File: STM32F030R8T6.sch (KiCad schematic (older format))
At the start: 1 part, among them U1 STM32F030R8Tx

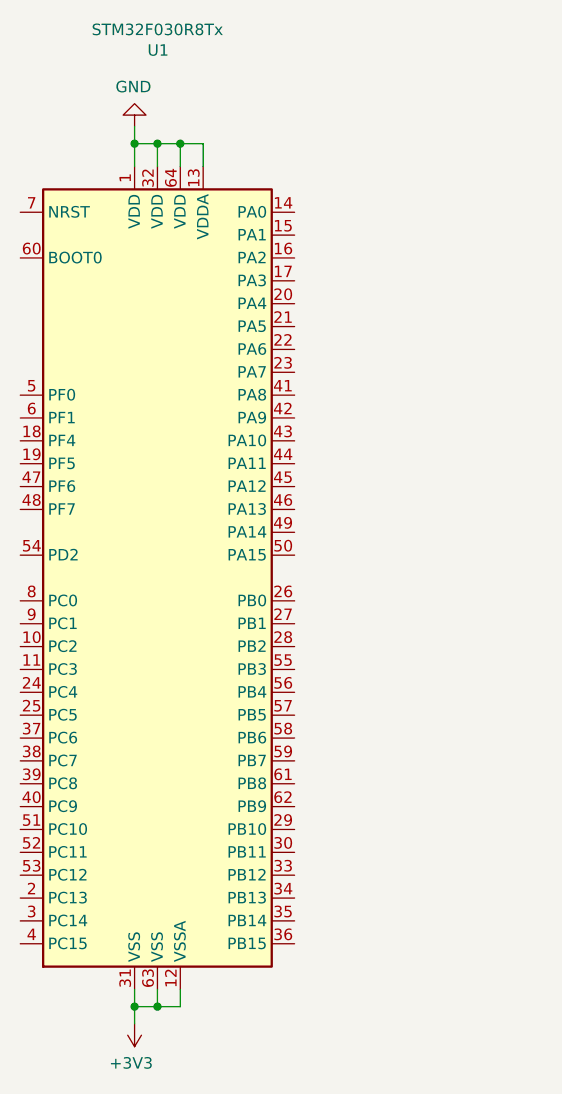
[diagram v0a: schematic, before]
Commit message: added some headers
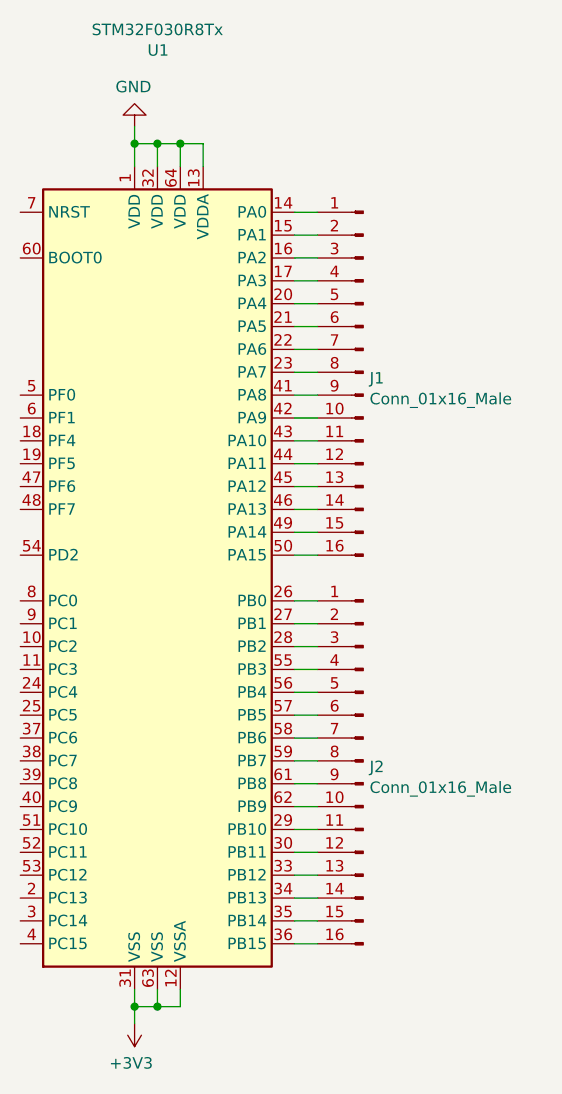
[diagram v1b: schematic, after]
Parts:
- added J1, J2: Conn_01x16_Male, Connector_PinHeader_2.54mm:PinHeader_1x16_P2.54mm_Vertical, symbol Connector:Conn_01x16_Male
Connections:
- net at U1.14 (PA0): now also J1.1 (Pin_1)
- net at U1.15 (PA1): now also J1.2 (Pin_2)
- net at U1.16 (PA2): now also J1.3 (Pin_3)
- net at U1.17 (PA3): now also J1.4 (Pin_4)
- net at U1.20 (PA4): now also J1.5 (Pin_5)
- net at U1.21 (PA5): now also J1.6 (Pin_6)
- net at U1.22 (PA6): now also J1.7 (Pin_7)
- net at U1.23 (PA7): now also J1.8 (Pin_8)
- net at U1.26 (PB0): now also J2.1 (Pin_1)
- net at U1.27 (PB1): now also J2.2 (Pin_2)
- net at U1.28 (PB2): now also J2.3 (Pin_3)
- net at U1.29 (PB10): now also J2.11 (Pin_11)
- net at U1.30 (PB11): now also J2.12 (Pin_12)
- net at U1.33 (PB12): now also J2.13 (Pin_13)
- net at U1.34 (PB13): now also J2.14 (Pin_14)
- net at U1.35 (PB14): now also J2.15 (Pin_15)
- net at U1.36 (PB15): now also J2.16 (Pin_16)
- net at U1.41 (PA8): now also J1.9 (Pin_9)
- net at U1.42 (PA9): now also J1.10 (Pin_10)
- net at U1.43 (PA10): now also J1.11 (Pin_11)
- net at U1.44 (PA11): now also J1.12 (Pin_12)
- net at U1.45 (PA12): now also J1.13 (Pin_13)
- net at U1.46 (PA13): now also J1.14 (Pin_14)
- net at U1.49 (PA14): now also J1.15 (Pin_15)
- net at U1.50 (PA15): now also J1.16 (Pin_16)
- net at U1.55 (PB3): now also J2.4 (Pin_4)
- net at U1.56 (PB4): now also J2.5 (Pin_5)
- net at U1.57 (PB5): now also J2.6 (Pin_6)
- net at U1.58 (PB6): now also J2.7 (Pin_7)
- net at U1.59 (PB7): now also J2.8 (Pin_8)
- net at U1.61 (PB8): now also J2.9 (Pin_9)
- net at U1.62 (PB9): now also J2.10 (Pin_10)
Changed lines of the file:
@@
 EESchema Schematic File Version 4
+LIBS:STM32F030R8T6-cache
 EELAYER 30 0
 EELAYER END
@@
 $EndComp
 $Comp
-L power:GND #PWR?
+L power:GND #PWR0101
 U 1 1 5E27E55C
 P 5550 1500
-F 0 "#PWR?" H 5550 1250 50  0001 C CNN
+F 0 "#PWR0101" H 5550 1250 50  0001 C CNN
 F 1 "GND" H 5555 1327 50  0000 C CNN
 F 2 "" H 5550 1500 50  0001 C CNN
@@
 $EndComp
 $Comp
-L power:+3V3 #PWR?
+L power:+3V3 #PWR0102
 U 1 1 5E27DFFF
 P 5550 5425
-F 0 "#PWR?" H 5550 5275 50  0001 C CNN
+F 0 "#PWR0102" H 5550 5275 50  0001 C CNN
 F 1 "+3V3" H 5565 5598 50  0000 C CNN
 F 2 "" H 5550 5425 50  0001 C CNN
@@
 	5750 5350 5650 5350
 Connection ~ 5650 5350
+$Comp
+L Connector:Conn_01x16_Male J1
+U 1 1 5E280BBC
+P 6550 2575
+F 0 "J1" H 6522 2549 50  0000 R CNN
+F 1 "Conn_01x16_Male" H 6522 2458 50  0000 R CNN
+F 2 "Connector_PinHeader_2.54mm:PinHeader_1x16_P2.54mm_Vertical" H 6550 2575 50  0001 C CNN
+F 3 "~" H 6550 2575 50  0001 C CNN
+	1    6550 2575
+	-1   0    0    -1
+$EndComp
+$Comp
+L Connector:Conn_01x16_Male J2
+U 1 1 5E2903A0
+P 6550 4275
+F 0 "J2" H 6522 4249 50  0000 R CNN
+F 1 "Conn_01x16_Male" H 6522 4158 50  0000 R CNN
+F 2 "Connector_PinHeader_2.54mm:PinHeader_1x16_P2.54mm_Vertical" H 6550 4275 50  0001 C CNN
+F 3 "~" H 6550 4275 50  0001 C CNN
+	1    6550 4275
+	-1   0    0    -1
+$EndComp
+Wire Wire Line
+	6250 3575 6350 3575
+Wire Wire Line
+	6350 3675 6250 3675
+Wire Wire Line
+	6250 3775 6350 3775
+Wire Wire Line
+	6250 5075 6350 5075
+Wire Wire Line
+	6350 4975 6250 4975
+Wire Wire Line
+	6250 4875 6350 4875
+Wire Wire Line
+	6350 4775 6250 4775
+Wire Wire Line
+	6250 4675 6350 4675
+Wire Wire Line
+	6350 4575 6250 4575
+Wire Wire Line
+	6250 4475 6350 4475
+Wire Wire Line
+	6250 4375 6350 4375
+Wire Wire Line
+	6350 4275 6250 4275
+Wire Wire Line
+	6250 4175 6350 4175
+Wire Wire Line
+	6350 4075 6250 4075
+Wire Wire Line
+	6250 3975 6350 3975
+Wire Wire Line
+	6350 3875 6250 3875
+Wire Wire Line
+	6350 3375 6250 3375
+Wire Wire Line
+	6350 3275 6250 3275
+Wire Wire Line
+	6250 3175 6350 3175
+Wire Wire Line
+	6350 3075 6250 3075
+Wire Wire Line
+	6250 2975 6350 2975
+Wire Wire Line
+	6350 2875 6250 2875
+Wire Wire Line
+	6250 2775 6350 2775
+Wire Wire Line
+	6250 2675 6350 2675
+Wire Wire Line
+	6350 2575 6250 2575
+Wire Wire Line
+	6250 2475 6350 2475
+Wire Wire Line
+	6350 2375 6250 2375
+Wire Wire Line
+	6250 2275 6350 2275
+Wire Wire Line
+	6350 2175 6250 2175
+Wire Wire Line
+	6250 2075 6350 2075
+Wire Wire Line
+	6350 1975 6250 1975
+Wire Wire Line
+	6250 1875 6350 1875
 $EndSCHEMATC
